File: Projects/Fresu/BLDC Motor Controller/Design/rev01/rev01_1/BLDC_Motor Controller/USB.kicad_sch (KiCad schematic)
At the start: 9 parts, among them J7 TYPE-C-31-M-12, U6 PUSB3AB6Z

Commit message: Update 15
Fixing some schematic errors

initial layout of larger component complete
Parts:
- renumbered J7 to J9, R57 to R61, R58 to R62, R61 to R64, R62 to R65, R60 to R66, R59 to R67
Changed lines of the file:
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@@
   (symbol (lib_id "Device:R") (at 160.02 85.09 270) (mirror x) (unit 1)
     (in_bom yes) (on_board yes) (dnp no)
-    (property "Reference" "R60" (at 160.02 82.55 90)
+    (property "Reference" "R66" (at 160.02 82.55 90)
       (effects (font (size 1.27 1.27)))
     )
@@
       (project "BLDC_Motor Controller"
         (path "/e63e39d7-6ac0-4ffd-8aa3-1841a4541b55/b75e002c-1f9d-4638-b120-9eb91151ad06"
-          (reference "R60") (unit 1)
+          (reference "R66") (unit 1)
         )
       )
@@
   (symbol (lib_id "Device:R") (at 135.89 86.36 0) (unit 1)
     (in_bom yes) (on_board yes) (dnp no)
-    (property "Reference" "R62" (at 138.43 86.36 90)
+    (property "Reference" "R65" (at 138.43 86.36 90)
       (effects (font (size 1.27 1.27)))
     )
@@
       (project "BLDC_Motor Controller"
         (path "/e63e39d7-6ac0-4ffd-8aa3-1841a4541b55/b75e002c-1f9d-4638-b120-9eb91151ad06"
-          (reference "R62") (unit 1)
+          (reference "R65") (unit 1)
         )
       )
@@
   (symbol (lib_id "power:GND") (at 173.99 67.31 0) (unit 1)
     (in_bom yes) (on_board yes) (dnp no)
-    (property "Reference" "#PWR096" (at 173.99 73.66 0)
+    (property "Reference" "#PWR0103" (at 173.99 73.66 0)
       (effects (font (size 1.27 1.27)) hide)
     )
@@
       (project "BLDC_Motor Controller"
         (path "/e63e39d7-6ac0-4ffd-8aa3-1841a4541b55/b75e002c-1f9d-4638-b120-9eb91151ad06"
-          (reference "#PWR096") (unit 1)
+          (reference "#PWR0103") (unit 1)
         )
       )
@@
   (symbol (lib_id "DF_ESC_Symbol_Library:USB_C_Receptacle_USB2.0") (at 86.36 88.9 0) (unit 1)
     (in_bom yes) (on_board yes) (dnp no) (fields_autoplaced)
-    (property "Reference" "J7" (at 86.36 66.04 0)
+    (property "Reference" "J9" (at 86.36 66.04 0)
       (effects (font (size 1.27 1.27)))
     )
@@
       (project "BLDC_Motor Controller"
         (path "/e63e39d7-6ac0-4ffd-8aa3-1841a4541b55/b75e002c-1f9d-4638-b120-9eb91151ad06"
-          (reference "J7") (unit 1)
+          (reference "J9") (unit 1)
         )
       )
@@
   (symbol (lib_id "Device:R") (at 128.27 88.9 0) (unit 1)
     (in_bom yes) (on_board yes) (dnp no)
-    (property "Reference" "R61" (at 130.81 88.9 90)
+    (property "Reference" "R64" (at 130.81 88.9 90)
       (effects (font (size 1.27 1.27)))
     )
@@
       (project "BLDC_Motor Controller"
         (path "/e63e39d7-6ac0-4ffd-8aa3-1841a4541b55/b75e002c-1f9d-4638-b120-9eb91151ad06"
-          (reference "R61") (unit 1)
+          (reference "R64") (unit 1)
         )
       )
@@
   (symbol (lib_id "Device:R") (at 160.02 93.98 270) (unit 1)
     (in_bom yes) (on_board yes) (dnp no)
-    (property "Reference" "R59" (at 160.02 96.52 90)
+    (property "Reference" "R67" (at 160.02 96.52 90)
       (effects (font (size 1.27 1.27)))
     )
@@
       (project "BLDC_Motor Controller"
         (path "/e63e39d7-6ac0-4ffd-8aa3-1841a4541b55/b75e002c-1f9d-4638-b120-9eb91151ad06"
-          (reference "R59") (unit 1)
+          (reference "R67") (unit 1)
         )
       )
@@
   (symbol (lib_id "power:GND") (at 128.27 95.25 0) (unit 1)
     (in_bom yes) (on_board yes) (dnp no) (fields_autoplaced)
-    (property "Reference" "#PWR097" (at 128.27 101.6 0)
+    (property "Reference" "#PWR0101" (at 128.27 101.6 0)
       (effects (font (size 1.27 1.27)) hide)
     )
@@
       (project "BLDC_Motor Controller"
         (path "/e63e39d7-6ac0-4ffd-8aa3-1841a4541b55/b75e002c-1f9d-4638-b120-9eb91151ad06"
-          (reference "#PWR097") (unit 1)
+          (reference "#PWR0101") (unit 1)
         )
       )
@@
   (symbol (lib_id "Device:R") (at 81.28 119.38 0) (mirror x) (unit 1)
     (in_bom yes) (on_board yes) (dnp no)
-    (property "Reference" "R58" (at 83.82 119.38 90)
+    (property "Reference" "R62" (at 83.82 119.38 90)
       (effects (font (size 1.27 1.27)))
     )
@@
       (project "BLDC_Motor Controller"
         (path "/e63e39d7-6ac0-4ffd-8aa3-1841a4541b55/b75e002c-1f9d-4638-b120-9eb91151ad06"
-          (reference "R58") (unit 1)
+          (reference "R62") (unit 1)
         )
       )
@@
   (symbol (lib_id "power:GND") (at 82.55 125.73 0) (unit 1)
     (in_bom yes) (on_board yes) (dnp no) (fields_autoplaced)
-    (property "Reference" "#PWR095" (at 82.55 132.08 0)
+    (property "Reference" "#PWR099" (at 82.55 132.08 0)
       (effects (font (size 1.27 1.27)) hide)
     )
@@
       (project "BLDC_Motor Controller"
         (path "/e63e39d7-6ac0-4ffd-8aa3-1841a4541b55/b75e002c-1f9d-4638-b120-9eb91151ad06"
-          (reference "#PWR095") (unit 1)
+          (reference "#PWR099") (unit 1)
         )
       )
@@
   (symbol (lib_id "Device:R") (at 77.47 119.38 180) (unit 1)
     (in_bom yes) (on_board yes) (dnp no)
-    (property "Reference" "R57" (at 74.93 119.38 90)
+    (property "Reference" "R61" (at 74.93 119.38 90)
       (effects (font (size 1.27 1.27)))
     )
@@
       (project "BLDC_Motor Controller"
         (path "/e63e39d7-6ac0-4ffd-8aa3-1841a4541b55/b75e002c-1f9d-4638-b120-9eb91151ad06"
-          (reference "R57") (unit 1)
+          (reference "R61") (unit 1)
         )
       )
@@
   (symbol (lib_id "power:GND") (at 135.89 92.71 0) (unit 1)
     (in_bom yes) (on_board yes) (dnp no) (fields_autoplaced)
-    (property "Reference" "#PWR098" (at 135.89 99.06 0)
+    (property "Reference" "#PWR0102" (at 135.89 99.06 0)
       (effects (font (size 1.27 1.27)) hide)
     )
@@
       (project "BLDC_Motor Controller"
         (path "/e63e39d7-6ac0-4ffd-8aa3-1841a4541b55/b75e002c-1f9d-4638-b120-9eb91151ad06"
-          (reference "#PWR098") (unit 1)
-        )
-      )
+          (reference "#PWR0102") (unit 1)
+        )
+      )

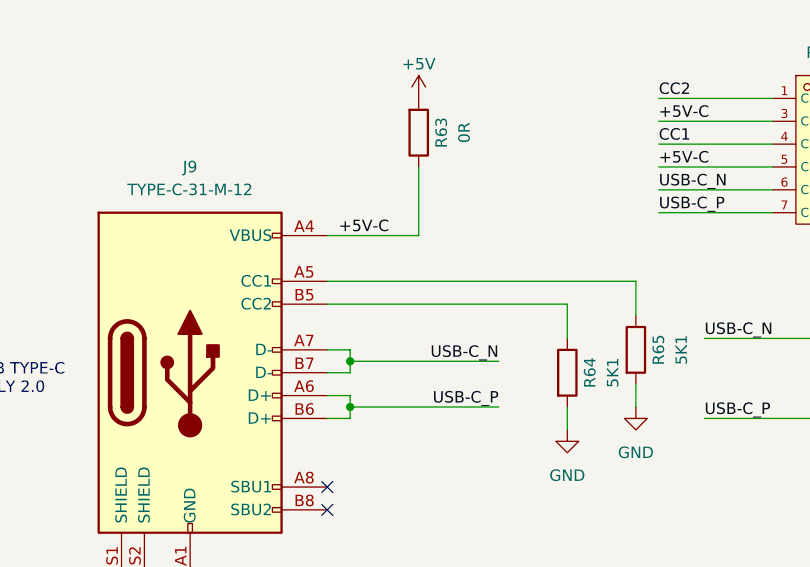
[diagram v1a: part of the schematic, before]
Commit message: Update 16
Almost finished placing all the components on the board as rough placement
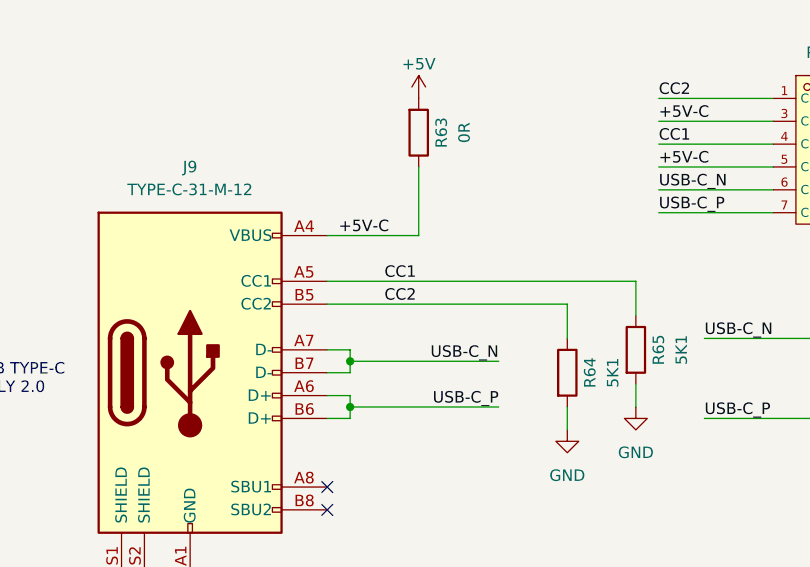
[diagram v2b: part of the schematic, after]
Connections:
- net CC1: now also J9.A5 (CC1), R65.1
- net CC2: now also J9.B5 (CC2), R64.1
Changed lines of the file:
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@@
+    (effects (font (size 1.27 1.27)) (justify left bottom))
+  )
+  (label "CC2" (at 107.95 81.28 0) (fields_autoplaced)
+    (effects (font (size 1.27 1.27)) (justify left bottom))
+  )
+  (label "CC1" (at 107.95 78.74 0) (fields_autoplaced)
     (effects (font (size 1.27 1.27)) (justify left bottom))
   )

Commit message: Update 26
Matched DF's Designators to mine so I can use BOM as is

Updated MFR'ing files

Rev1 Ready for release
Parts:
- renumbered U6 to CR1, J9 to J10, R62 to R54, R63 to R55, R64 to R56, R65 to R57, R61 to R60
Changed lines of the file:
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@@
 		(on_board yes)
 		(dnp no)
-		(property "Reference" "R65"
+		(property "Reference" "R57"
 			(at 138.43 86.36 90)
 			(effects
@@
 			(project "BLDC_Motor Controller"
 				(path "/e63e39d7-6ac0-4ffd-8aa3-1841a4541b55/b75e002c-1f9d-4638-b120-9eb91151ad06"
-					(reference "R65")
+					(reference "R57")
 					(unit 1)
 				)
@@
 		(dnp no)
 		(fields_autoplaced yes)
-		(property "Reference" "J9"
+		(property "Reference" "J10"
 			(at 86.36 66.04 0)
 			(effects
@@
 			(project "BLDC_Motor Controller"
 				(path "/e63e39d7-6ac0-4ffd-8aa3-1841a4541b55/b75e002c-1f9d-4638-b120-9eb91151ad06"
-					(reference "J9")
+					(reference "J10")
 					(unit 1)
 				)
@@
 		(on_board yes)
 		(dnp no)
-		(property "Reference" "R64"
+		(property "Reference" "R56"
 			(at 130.81 88.9 90)
 			(effects
@@
 			(project "BLDC_Motor Controller"
 				(path "/e63e39d7-6ac0-4ffd-8aa3-1841a4541b55/b75e002c-1f9d-4638-b120-9eb91151ad06"
-					(reference "R64")
+					(reference "R56")
 					(unit 1)
 				)
@@
 		(dnp no)
 		(fields_autoplaced yes)
-		(property "Reference" "U6"
+		(property "Reference" "CR1"
 			(at 160.02 50.8 0)
 			(effects
@@
 			(project "BLDC_Motor Controller"
 				(path "/e63e39d7-6ac0-4ffd-8aa3-1841a4541b55/b75e002c-1f9d-4638-b120-9eb91151ad06"
-					(reference "U6")
+					(reference "CR1")
 					(unit 1)
 				)
@@
 		(on_board yes)
 		(dnp no)
-		(property "Reference" "R62"
+		(property "Reference" "R54"
 			(at 83.82 119.38 90)
 			(effects
@@
 			(project "BLDC_Motor Controller"
 				(path "/e63e39d7-6ac0-4ffd-8aa3-1841a4541b55/b75e002c-1f9d-4638-b120-9eb91151ad06"
-					(reference "R62")
+					(reference "R54")
 					(unit 1)
 				)
@@
 		(on_board yes)
 		(dnp no)
-		(property "Reference" "R61"
+		(property "Reference" "R60"
 			(at 74.93 119.38 90)
 			(effects
@@
 			(project "BLDC_Motor Controller"
 				(path "/e63e39d7-6ac0-4ffd-8aa3-1841a4541b55/b75e002c-1f9d-4638-b120-9eb91151ad06"
-					(reference "R61")
+					(reference "R60")
 					(unit 1)
 				)
@@
 		(on_board yes)
 		(dnp no)
-		(property "Reference" "R63"
+		(property "Reference" "R55"
 			(at 114.3 62.23 90)
 			(effects
@@
 			(project "BLDC_Motor Controller"
 				(path "/e63e39d7-6ac0-4ffd-8aa3-1841a4541b55/b75e002c-1f9d-4638-b120-9eb91151ad06"
-					(reference "R63")
-					(unit 1)
-				)
+					(reference "R55")
+					(unit 1)
+				)
